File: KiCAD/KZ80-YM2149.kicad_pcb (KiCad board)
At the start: 2 copper layers, 100 x 74 mm, 39 parts, among them J1 Audio-Jack-3_2Switches, J2 ADDR JP, J3 JOYSTICK1, J4 SBC8080 BUS, J5 JOYSTICK2, U1 74HC138, U2 74HC00, U3 74HC02, U4 74HC157, U5 74HC74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

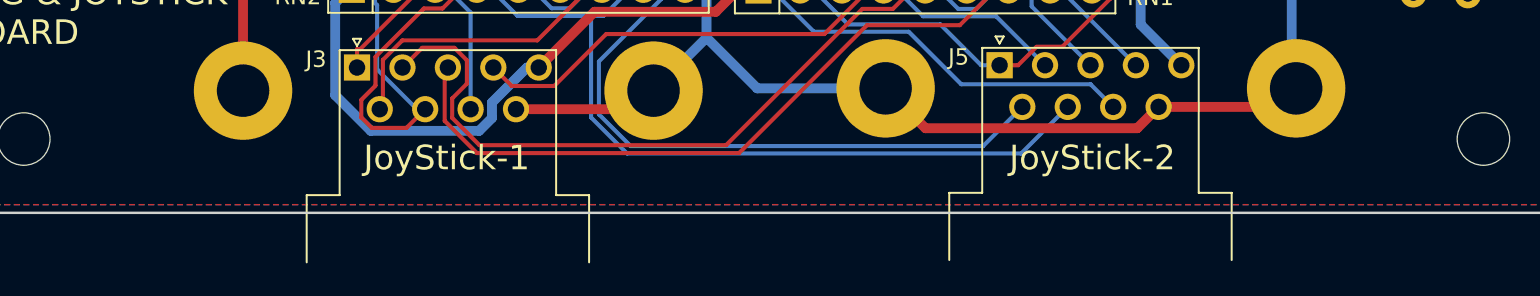
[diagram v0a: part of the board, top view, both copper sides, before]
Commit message: ジョイスティック シルク追加
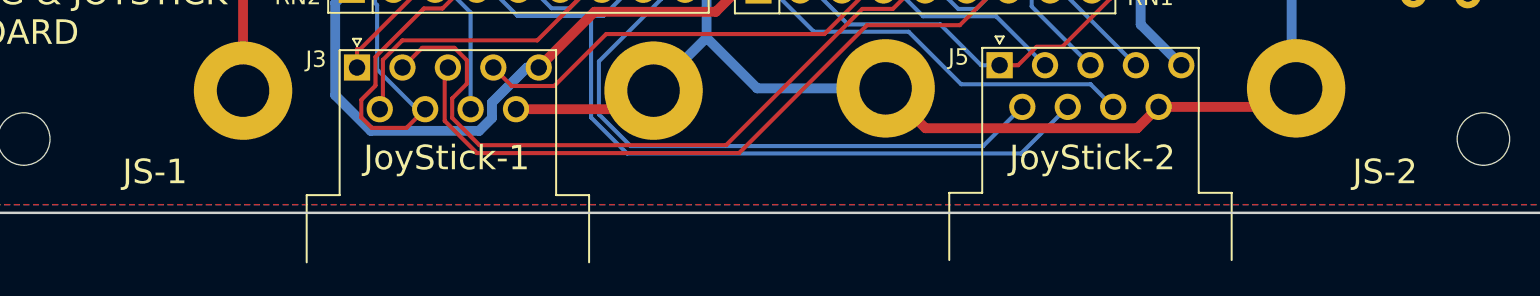
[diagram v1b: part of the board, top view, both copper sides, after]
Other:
- board text added: "JS-1"
- board text added: "JS-2"
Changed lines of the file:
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@@
   (general
     (thickness 1.6)
-    (drawings 23)
+    (drawings 25)
     (tracks 864)
     (zones 0)
@@
     )
   )
+  (gr_text JS-2 (at 178.5 121.5) (layer F.SilkS)
+    (effects (font (size 1.5 1.5) (thickness 0.3)))
+  )
+  (gr_text JS-1 (at 103.5 121.5) (layer F.SilkS)
+    (effects (font (size 1.5 1.5) (thickness 0.3)))
+  )
   (gr_text JoyStick-2 (at 160.655 120.65) (layer F.SilkS)

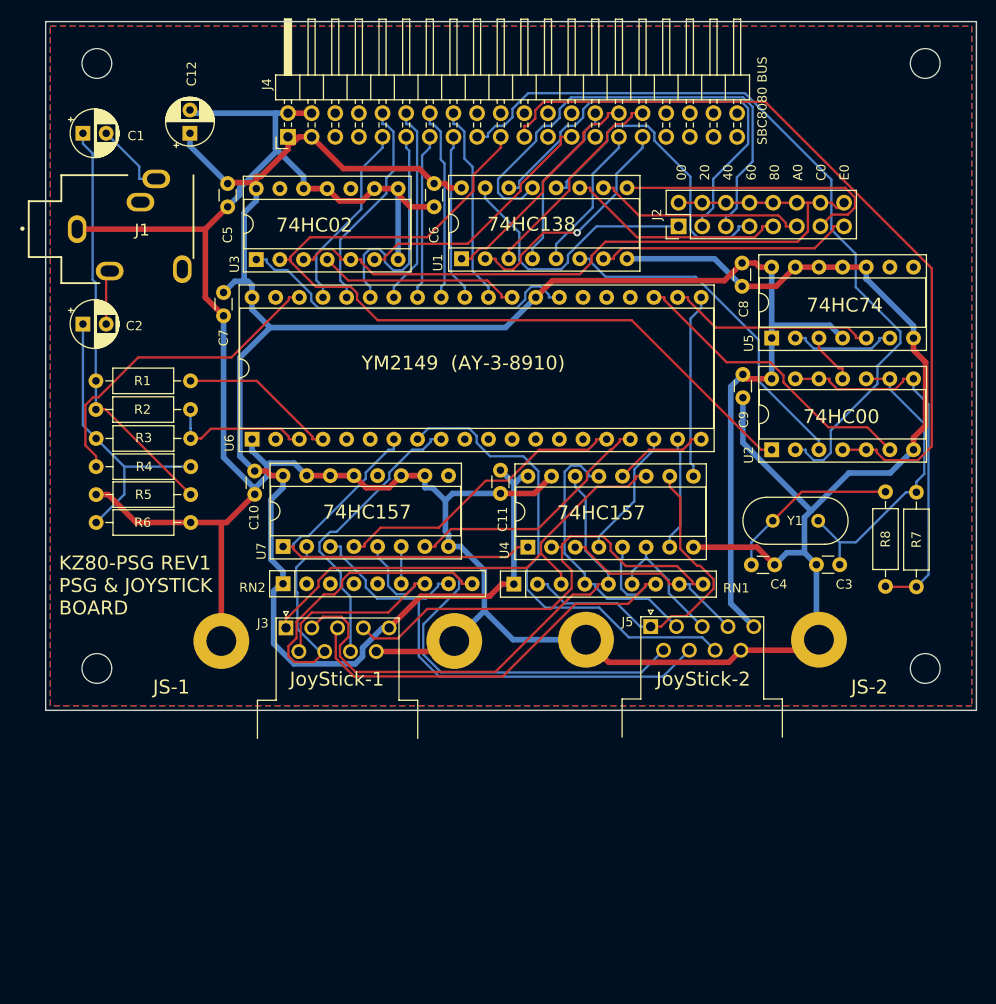
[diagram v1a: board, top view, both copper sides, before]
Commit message: REV2基板 回路回路、パターン作成・ガーバー出力
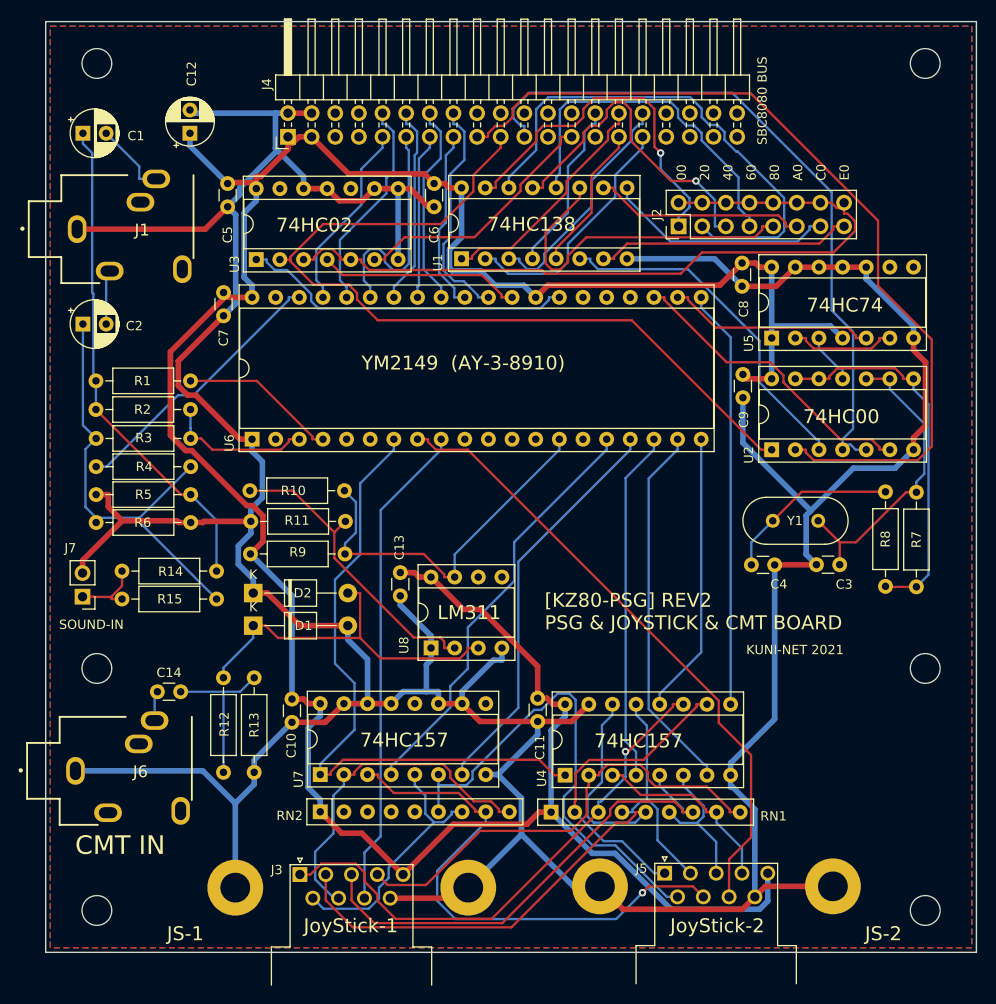
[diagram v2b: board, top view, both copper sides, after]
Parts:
- added C13: 0.1u, Capacitor_THT:C_Disc_D3.0mm_W1.6mm_P2.50mm, F.Cu at (128.1, 109.2)
- added C14: 0.1u, Capacitor_THT:C_Disc_D3.0mm_W1.6mm_P2.50mm, F.Cu at (102.0, 122.0)
- added D1: 1N4148, Diode_THT:D_T-1_P10.16mm_Horizontal, F.Cu at (112.3, 114.9)
- added D2: 1N4148, Diode_THT:D_T-1_P10.16mm_Horizontal, F.Cu at (112.3, 111.4)
- added J6: CMT IN, AJ-1780:AJ-1780, F.Cu at (91.5, 130.5)
- added J7: SOUND-IN, Connector_PinHeader_2.54mm:PinHeader_1x02_P2.54mm_Vertical, F.Cu at (94.0, 111.8)
- added MH5: MountingHole, MountingHole:MountingHole_3.2mm_M3, F.Cu at (95.5, 145.5)
- added MH6: MountingHole, MountingHole:MountingHole_3.2mm_M3, F.Cu at (184.5, 145.5)
- added R10: 470k, Resistor_THT:R_Axial_DIN0207_L6.3mm_D2.5mm_P10.16mm_Horizontal, F.Cu at (122.1, 100.4)
- added R11: 4.7k, Resistor_THT:R_Axial_DIN0207_L6.3mm_D2.5mm_P10.16mm_Horizontal, F.Cu at (122.2, 103.7)
- added R12: 12k, Resistor_THT:R_Axial_DIN0207_L6.3mm_D2.5mm_P10.16mm_Horizontal, F.Cu at (109.1, 120.5)
- added R13: 2.2k, Resistor_THT:R_Axial_DIN0207_L6.3mm_D2.5mm_P10.16mm_Horizontal, F.Cu at (112.4, 120.5)
- added R14: 2.2k, Resistor_THT:R_Axial_DIN0207_L6.3mm_D2.5mm_P10.16mm_Horizontal, F.Cu at (108.4, 109.0)
- added R15: 2.2k, Resistor_THT:R_Axial_DIN0207_L6.3mm_D2.5mm_P10.16mm_Horizontal, F.Cu at (108.4, 112.0)
- added R9: 2.2k, Resistor_THT:R_Axial_DIN0207_L6.3mm_D2.5mm_P10.16mm_Horizontal, F.Cu at (112.0, 107.2)
- added U8: LM311, Package_DIP:DIP-8_W7.62mm_Socket, F.Cu at (131.4, 117.3)
- Y1: value 3.57MHz -> 3.579545MHz
- moved J5 26.5 mm to (156.5, 141.5)
- moved J3 26.5 mm to (117.3, 141.6)
- moved C10 24.8 mm to (116.5, 122.8)
- moved C11 24.8 mm to (142.9, 122.7)
- moved RN1 24.8 mm to (144.3, 134.9)
- moved RN2 24.8 mm to (119.5, 134.9)
- moved U4 24.8 mm to (145.8, 131.0)
- moved U7 24.8 mm to (119.5, 130.9)
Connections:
- U6 pad 14: (no net) -> /IOA7
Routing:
- net GND: track 351.6 -> 465.2 mm
- net /IOA7: track 0.00 -> 40.2 mm
- net VCC: track 253.2 -> 292.9 mm
- net Net-(D1-Pad1): track 0.00 -> 39.3 mm
- net Net-(R10-Pad2): track 0.00 -> 32.7 mm
- net Net-(U4-Pad7): track 12.2 -> 40.1 mm
- net Net-(U4-Pad9): track 19.8 -> 45.0 mm
- net Net-(U4-Pad4): track 14.1 -> 37.8 mm
- net Net-(U4-Pad1): track 45.3 -> 68.9 mm
- net Net-(J3-Pad8): track 31.3 -> 52.7 mm
- net Net-(U4-Pad12): track 10.3 -> 30.3 mm
- net Net-(J2-Pad5): track 52.6 -> 35.1 mm, vias 0 -> 1
- net Net-(C14-Pad2): track 0.00 -> 17.2 mm
- net Net-(U6-Pad17): track 27.5 -> 43.5 mm
- net Net-(C2-Pad1): track 31.5 -> 47.4 mm
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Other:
- board size 100 x 74 mm -> 100 x 100 mm
- board text added: "CMT IN"
- board text added: "KUNI-NET 2021"
- board text added: "LM311"
- board text added: "SOUND-IN"
- board text added: "[KZ80-PSG] REV2 PSG & JOYSTICK & CMT BOARD"
- board text removed: "KZ80-PSG REV1 PSG & JOYSTICK BOARD"

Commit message: 回路図間違い修正・ガーバー再出力
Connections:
- J6 pad 2: Net-(C14-Pad1) -> (no net)
- J6 pad 5: (no net) -> Net-(C14-Pad1)
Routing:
- net Net-(C14-Pad1): track 3.22 -> 17.0 mm
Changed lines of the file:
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@@
     (thickness 1.6)
     (drawings 31)
-    (tracks 964)
+    (tracks 968)
     (zones 0)
     (modules 55)
@@
     (fp_line (start 14.2 -5.8) (end 14.2 5.8) (layer Dwgs.User) (width 0.2))
     (fp_line (start 0 -5.8) (end 14.2 -5.8) (layer Dwgs.User) (width 0.2))
-    (pad 5 thru_hole oval (at 5.2 4.5 90) (size 2 3) (drill oval 1.2 2) (layers *.Cu *.Mask F.SilkS))
+    (pad 5 thru_hole oval (at 5.2 4.5 90) (size 2 3) (drill oval 1.2 2) (layers *.Cu *.Mask F.SilkS)
+      (net 68 "Net-(C14-Pad1)"))
     (pad 4 thru_hole oval (at 13 4.3 90) (size 3 2) (drill oval 2 1.2) (layers *.Cu *.Mask F.SilkS))
     (pad 3 thru_hole oval (at 8.5 -2.9 90) (size 2 3) (drill oval 1.2 2) (layers *.Cu *.Mask F.SilkS))
-    (pad 2 thru_hole oval (at 10.2 -5.4 90) (size 2 3) (drill oval 1.2 2) (layers *.Cu *.Mask F.SilkS)
-      (net 68 "Net-(C14-Pad1)"))
+    (pad 2 thru_hole oval (at 10.2 -5.4 90) (size 2 3) (drill oval 1.2 2) (layers *.Cu *.Mask F.SilkS))
     (pad 1 thru_hole oval (at 1.7 0 90) (size 3 2) (drill oval 2 1.2) (layers *.Cu *.Mask F.SilkS)
       (net 2 GND))
@@
   (segment (start 109.1 130.66) (end 109.1 129.5347) (width 0.25) (layer B.Cu) (net 67))
   (segment (start 102 122) (end 101.7 122.3) (width 0.25) (layer B.Cu) (net 68))
-  (segment (start 101.7 122.3) (end 101.7 125.1) (width 0.25) (layer B.Cu) (net 68))
+  (segment (start 100.86863 122) (end 100.78863 121.92) (width 0.25) (layer F.Cu) (net 68))
+  (segment (start 102 122) (end 100.86863 122) (width 0.25) (layer F.Cu) (net 68))
+  (segment (start 100.78863 121.92) (end 99.82 121.92) (width 0.25) (layer F.Cu) (net 68))
+  (segment (start 96.7 125.04) (end 96.7 135) (width 0.25) (layer F.Cu) (net 68))
+  (segment (start 99.82 121.92) (end 96.7 125.04) (width 0.25) (layer F.Cu) (net 68))
   (segment (start 112.3 114.9) (end 113.6253 114.9) (width 0.25) (layer F.Cu) (net 69))
   (segment (start 123.7853 116.2252) (end 123.7852 116.2253) (width 0.25) (layer F.Cu) (net 69))

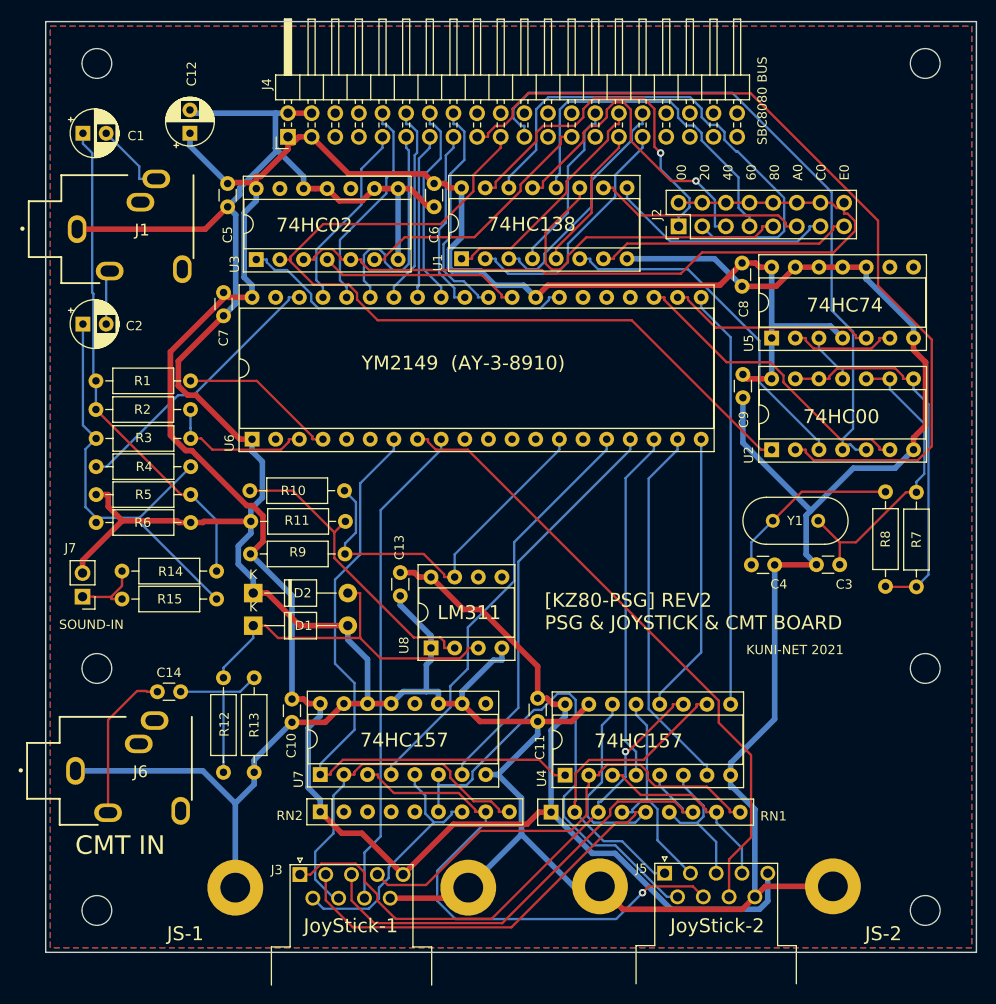
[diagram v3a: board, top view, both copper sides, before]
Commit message: KiCAD6対応 & CMTステレオジャック回路修正 ・ガーバー2.1出力 #2
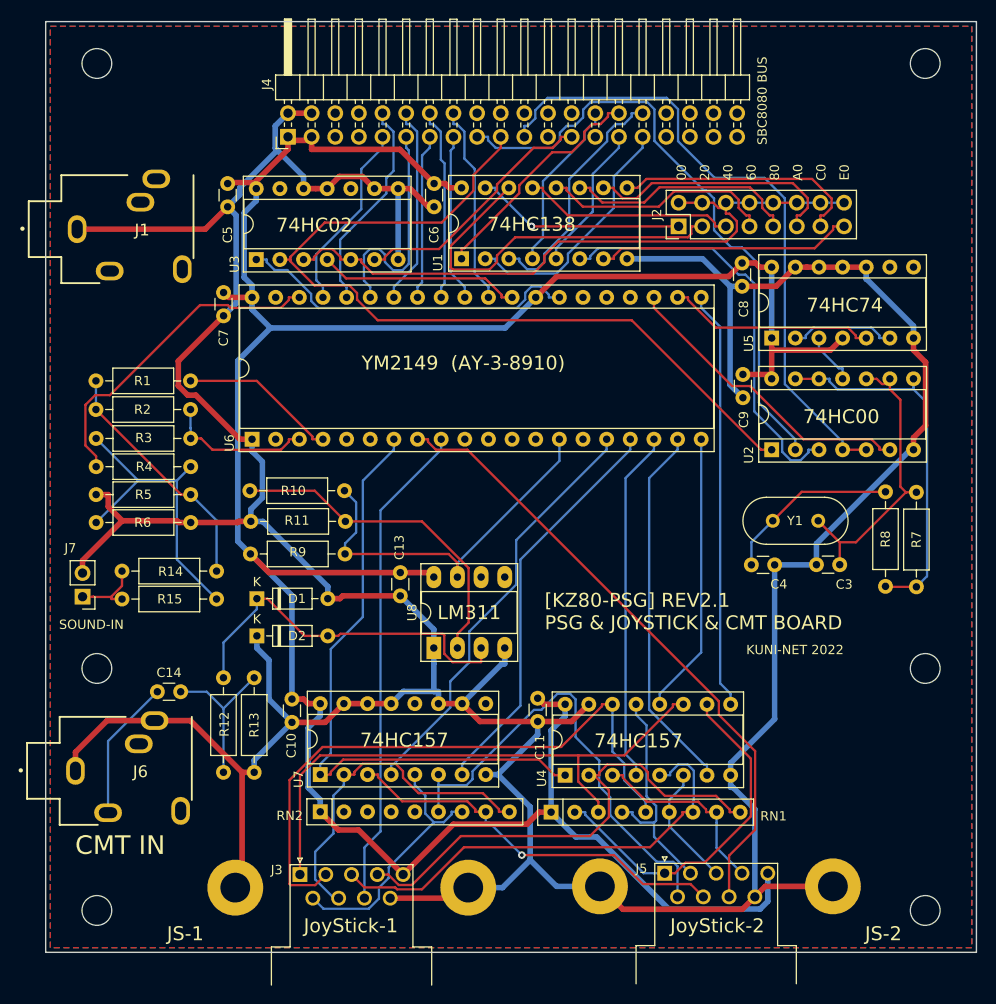
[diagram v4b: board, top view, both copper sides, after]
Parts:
- removed C1, C2: 1u, Capacitor_THT:CP_Radial_D5.0mm_P2.50mm
- removed C12: 10u, Capacitor_THT:CP_Radial_D5.0mm_P2.50mm
- D1, D2: footprint Diode_THT:D_T-1_P10.16mm_Horizontal -> Diode_THT:D_DO-35_SOD27_P7.62mm_Horizontal
- U8: footprint Package_DIP:DIP-8_W7.62mm_Socket -> Package_DIP:DIP-8_W7.62mm_Socket_LongPads
- moved D2 4.62 mm to (112.7, 116.0)
- moved D1 2.93 mm to (112.7, 112.0)
- moved U8 0.30 mm to (131.7, 117.3)
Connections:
- net /~IORD renamed /~{IORD}
- net /~IOWR renamed /~{IOWR}
- J1 pad 2: Net-(C1-Pad2) -> unconnected-(J1-Pad2)
- J1 pad 3: (no net) -> unconnected-(J1-Pad3)
- J1 pad 4: (no net) -> unconnected-(J1-Pad4)
- J1 pad 5: Net-(C2-Pad2) -> unconnected-(J1-Pad5)
- J4 pad 18: (no net) -> unconnected-(J4-Pad18)
- J4 pad 20: (no net) -> unconnected-(J4-Pad20)
- J4 pad 22: (no net) -> unconnected-(J4-Pad22)
- J4 pad 23: (no net) -> unconnected-(J4-Pad23)
- J4 pad 24: (no net) -> unconnected-(J4-Pad24)
- J4 pad 26: (no net) -> unconnected-(J4-Pad26)
- J4 pad 27: (no net) -> unconnected-(J4-Pad27)
- J4 pad 33: (no net) -> unconnected-(J4-Pad33)
- J4 pad 34: (no net) -> unconnected-(J4-Pad34)
- J4 pad 35: (no net) -> unconnected-(J4-Pad35)
- J4 pad 36: (no net) -> unconnected-(J4-Pad36)
- J4 pad 37: (no net) -> unconnected-(J4-Pad37)
- J4 pad 38: (no net) -> unconnected-(J4-Pad38)
- J4 pad 39: (no net) -> unconnected-(J4-Pad39)
- J4 pad 40: (no net) -> unconnected-(J4-Pad40)
- J4 pad 5: (no net) -> unconnected-(J4-Pad5)
- J4 pad 6: (no net) -> unconnected-(J4-Pad6)
- J4 pad 7: (no net) -> unconnected-(J4-Pad7)
- J4 pad 8: (no net) -> unconnected-(J4-Pad8)
- J6 pad 2: (no net) -> GND
- J6 pad 3: (no net) -> unconnected-(J6-Pad3)
- J6 pad 4: (no net) -> unconnected-(J6-Pad4)
- RN2 pad 2: (no net) -> unconnected-(RN2-Pad2)
- RN2 pad 3: (no net) -> unconnected-(RN2-Pad3)
- RN2 pad 4: (no net) -> unconnected-(RN2-Pad4)
- RN2 pad 5: (no net) -> unconnected-(RN2-Pad5)
- U3 pad 10: (no net) -> unconnected-(U3-Pad10)
- U3 pad 13: (no net) -> unconnected-(U3-Pad13)
- U5 pad 8: (no net) -> unconnected-(U5-Pad8)
- U5 pad 9: (no net) -> unconnected-(U5-Pad9)
- U6 pad 10: (no net) -> unconnected-(U6-Pad10)
- U6 pad 11: (no net) -> unconnected-(U6-Pad11)
- U6 pad 12: (no net) -> unconnected-(U6-Pad12)
- U6 pad 13: (no net) -> unconnected-(U6-Pad13)
- U6 pad 15: (no net) -> unconnected-(U6-Pad15)
- U6 pad 24: (no net) -> unconnected-(U6-Pad24)
- U6 pad 25: (no net) -> unconnected-(U6-Pad25)
- U6 pad 26: (no net) -> unconnected-(U6-Pad26)
- U6 pad 39: (no net) -> unconnected-(U6-Pad39)
- U6 pad 6: (no net) -> unconnected-(U6-Pad6)
- U7 pad 12: (no net) -> unconnected-(U7-Pad12)
- U7 pad 9: (no net) -> unconnected-(U7-Pad9)
- U8 pad 5: (no net) -> unconnected-(U8-Pad5)
- U8 pad 6: (no net) -> unconnected-(U8-Pad6)
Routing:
- net /~{IORD}: track 94.0 -> 66.8 mm
- net Net-(R1-Pad1): track 53.6 -> 26.4 mm
- net Net-(J2-Pad1): track 38.9 -> 22.7 mm
- net Net-(J5-Pad7): track 57.7 -> 42.5 mm
- net Net-(J2-Pad3): track 55.5 -> 41.1 mm
- net Net-(R15-Pad1): track 47.4 -> 33.5 mm
- net Net-(J2-Pad7): track 38.4 -> 25.2 mm
- net Net-(J2-Pad5): track 35.1 -> 22.9 mm, vias 1 -> 0
- net Net-(J2-Pad10): track 84.9 -> 72.7 mm
- net Net-(J2-Pad9): track 36.9 -> 25.2 mm
- net GND: track 465.2 -> 456.9 mm
- net Net-(C1-Pad2): track 8.20 -> 0.00 mm
- net Net-(U1-Pad6): track 37.6 -> 45.2 mm
- net Net-(C2-Pad2): track 5.86 -> 0.00 mm
- net Net-(R4-Pad2): track 29.5 -> 35.3 mm
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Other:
- net class BOLD removed
- net class Default removed
- board text added: "KUNI-NET 2022"
- board text added: "[KZ80-PSG] REV2.1 PSG & JOYSTICK & CMT BOARD"
- board text removed: "KUNI-NET 2021"
- board text removed: "[KZ80-PSG] REV2 PSG & JOYSTICK & CMT BOARD"

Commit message: コンデンサシンボル変更忘れ対応 #2
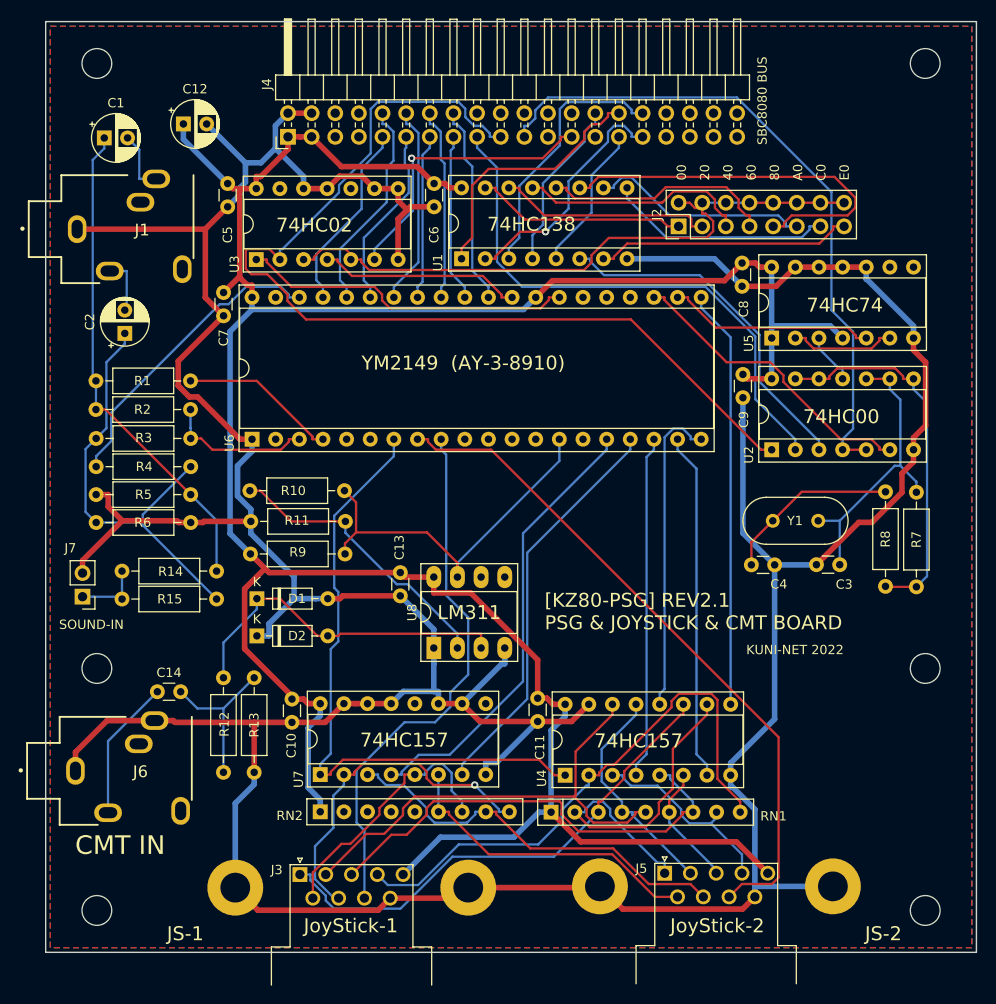
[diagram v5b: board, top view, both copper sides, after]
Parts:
- added C1: 1u, Capacitor_THT:CP_Radial_D5.0mm_P2.50mm, F.Cu at (96.3, 62.5)
- added C12: 10u, Capacitor_THT:CP_Radial_D5.0mm_P2.50mm, F.Cu at (104.8, 61.0)
- added C2: 1u, Capacitor_THT:CP_Radial_D5.0mm_P2.50mm, F.Cu at (98.5, 83.5)
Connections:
- J1 pad 2: unconnected-(J1-Pad2) -> Net-(J1-Pad2)
- J1 pad 5: unconnected-(J1-Pad5) -> Net-(J1-Pad5)
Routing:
- net Net-(R1-Pad1): track 26.4 -> 53.2 mm
- net Net-(J2-Pad3): track 41.1 -> 23.1 mm
- net Net-(J2-Pad9): track 25.2 -> 42.1 mm
- net Net-(J5-Pad6): track 50.3 -> 33.6 mm
- net /~{IOWR}: track 91.7 -> 108.1 mm
- net Net-(J3-Pad2): track 66.8 -> 52.1 mm
- net GND: track 456.9 -> 470.6 mm
- net Net-(R15-Pad1): track 33.5 -> 47.2 mm
- net VCC: track 289.1 -> 299.5 mm
- net Net-(J3-Pad1): track 62.2 -> 54.3 mm
- net Net-(J3-Pad4): track 53.1 -> 60.8 mm
- net /~{IORD}: track 66.8 -> 59.3 mm
- net Net-(U1-Pad6): track 45.2 -> 38.0 mm
- net Net-(J1-Pad2): track 0.00 -> 6.75 mm
- net Net-(J1-Pad5): track 0.00 -> 6.11 mm
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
